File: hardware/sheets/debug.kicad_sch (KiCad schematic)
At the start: 0 parts

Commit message: hw: draw MCU module and debug sheets (#6)
* hw: draw MCU module and debug sheets

Draw the MDBT53-P1M with Raytac's normal-voltage DC/DC reference
circuit (Ver.E section 8.1.2): VDD and VDDH on 3V3 with 4.7 uF, a
10 uH inductor and 1 uF on each internal regulator output, and module
VBUS through 2.2 ohm with 4.7 uF. The 32.768 kHz crystal uses the
nRF5340's internal 9 pF load, with external load caps left unfitted.
USB D+/D- reach the module through 0 ohm links that can take the
27 ohm resistors shown in Raytac's figure.

The debug sheet has the ARM Cortex 10-pin SWD header and pads for
reset, SWD, UART, ground and six spare GPIO. The header connects to
the nRF5340 DK's debug out; pin 3 is grounded so the DK selects the
external target.

Labels whose other end belongs on a sheet not drawn yet are excluded
from ERC with a comment naming that sheet, to be removed as each
sheet is drawn.

* docs: describe the module supply and debug setup

Record the module's reference-circuit parts, the 0 ohm USB data links
and the SWD header in the hardware overview. State the DC/DC inductor
limits as TDK specifies them: 90 mA maximum for at most a 50%
inductance drop, with 250 mA only a typical temperature-rise
reference, against Nordic's reference BOM.

Debugging uses the nRF5340 DK's debug out. Nordic requires the target
voltage to match the DK, which runs at 3 V on USB alone, so bring-up
supplies the DK's nRF5340 with 3.3 V on its external input and checks
that the two voltages match before connecting. Bring-up also checks
the module's DC/DC regulators.

* ci: avoid SIGPIPE when printing host tool versions

Under pipefail, `--version | head -n 1` can fail the host-dependency
script when head exits before the tool finishes writing. Capture the
whole version output and print its first line instead.
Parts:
- added J501: SWD 2x5 1.27mm, Connector_PinHeader_1.27mm:PinHeader_2x05_P1.27mm_Vertical_SMD, symbol Connector:Conn_ARM_JTAG_SWD_10
- added TP501: nRESET, TestPoint:TestPoint_Pad_D1.0mm, symbol Connector:TestPoint
- added TP502: SWDIO, TestPoint:TestPoint_Pad_D1.0mm, symbol Connector:TestPoint
- added TP503: SWDCLK, TestPoint:TestPoint_Pad_D1.0mm, symbol Connector:TestPoint
- added TP504: UART_TX, TestPoint:TestPoint_Pad_D1.0mm, symbol Connector:TestPoint
- added TP505: UART_RX, TestPoint:TestPoint_Pad_D1.0mm, symbol Connector:TestPoint
- added TP506: GND, TestPoint:TestPoint_Pad_D1.0mm, symbol Connector:TestPoint
- added TP507: P0.02, TestPoint:TestPoint_Pad_D1.0mm, symbol Connector:TestPoint
- added TP508: P0.03, TestPoint:TestPoint_Pad_D1.0mm, symbol Connector:TestPoint
- added TP509: P0.13, TestPoint:TestPoint_Pad_D1.0mm, symbol Connector:TestPoint
- added TP510: P0.14, TestPoint:TestPoint_Pad_D1.0mm, symbol Connector:TestPoint
- added TP511: P0.26/AIN5, TestPoint:TestPoint_Pad_D1.0mm, symbol Connector:TestPoint
- added TP512: P0.27/AIN6, TestPoint:TestPoint_Pad_D1.0mm, symbol Connector:TestPoint
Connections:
- new net +3V3: J501.1 (VTref)
- new net GND: J501.3 (GND), J501.5 (GND), J501.9 (GNDDetect), TP506.1
- new net SPARE_P0_02: TP507.1
- new net SPARE_P0_03: TP508.1
- new net SPARE_P0_13: TP509.1
- new net SPARE_P0_14: TP510.1
- new net SPARE_P0_26: TP511.1
- new net SPARE_P0_27: TP512.1
- new net SWDCLK: J501.4 (SWCLK/TCK), TP503.1
- new net SWDIO: J501.2 (SWDIO/TMS), TP502.1
- new net UART_RX: TP505.1
- new net UART_TX: TP504.1
- new net nRESET: J501.10 (~{RESET}), TP501.1
- no-connect marks 0 -> 2
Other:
- note added: "Debug (Rev A) - design notes J501: ARM Cortex 10-pin SWD header (2 x 5, 1.27 mm) to the nRF5340 DK debug out (P19) by a 10-pin flat cable. Pin 3 = GND selects the external target. Voltages must match: run the DK at 3.3 V from P21 (SW10 VEXT->nRF ON, SW9 = VDD; DK on USB alone is 3.0 V). Keep DK SB47 open so P19 pin 1 does not drive the badge 3V3. VTref = 3V3; nRESET has the module's internal pull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"

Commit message: hw: apply layout footprint and test-point changes to the schematic
The matrix LEDs use the KENTO-pattern footprint, L1101 the PCB coil,
MK1001 the 0.6 mm hole footprint and J301 the project HRO copy.

Removes test points that duplicate others: TP303 and TP304, TP208 and
TP506, and TP501-TP503, whose signals are on the SWD header. Also
removes H1304, which the carrier does not use. Rail and GND test points
move to 0.8 mm pads.

nRESET now connects only the header's open-collector pin and the module
input. ERC reports that as not driven, so the error is excluded: the
nRF5340 has an internal pull-up on reset.
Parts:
- removed TP501: nRESET, TestPoint:TestPoint_Pad_D1.0mm, symbol Connector:TestPoint
- removed TP502: SWDIO, TestPoint:TestPoint_Pad_D1.0mm, symbol Connector:TestPoint
- removed TP503: SWDCLK, TestPoint:TestPoint_Pad_D1.0mm, symbol Connector:TestPoint
- removed TP506: GND, TestPoint:TestPoint_Pad_D1.0mm, symbol Connector:TestPoint

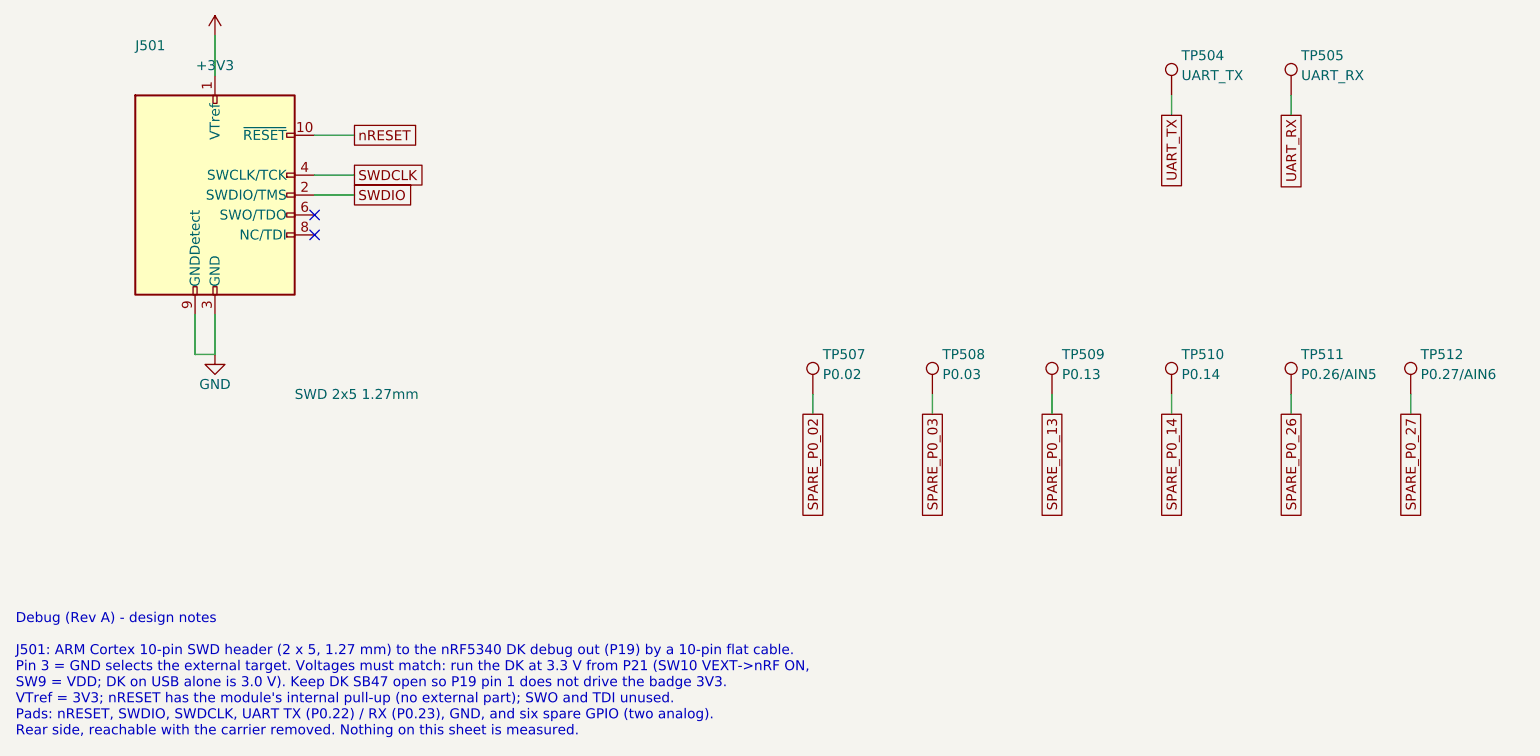
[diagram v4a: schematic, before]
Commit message: hw: switch U401 to the E73 nRF52840 module
The MDBT53-P1M cannot be sourced in time for the Rev A order, while
the E73-2G4M08S1C is stocked at JLCPCB (ADR 0015).

The E73 holds its DC/DC inductors and decoupling, so L401/L402 and
C403/C404 are removed. The nRF52840 has no internal 32.768 kHz load,
so C405/C406 are fitted with 12 pF; the value is calculated and still
needs checking against the Product Specification. All 29 module GPIO
are used: CHG_STAT is no longer read by the MCU, and the UART pads,
spare GPIO pads and IMU SPI-fallback links are removed. Pins Ebyte
marks as low-frequency carry only analog inputs or slow signals.
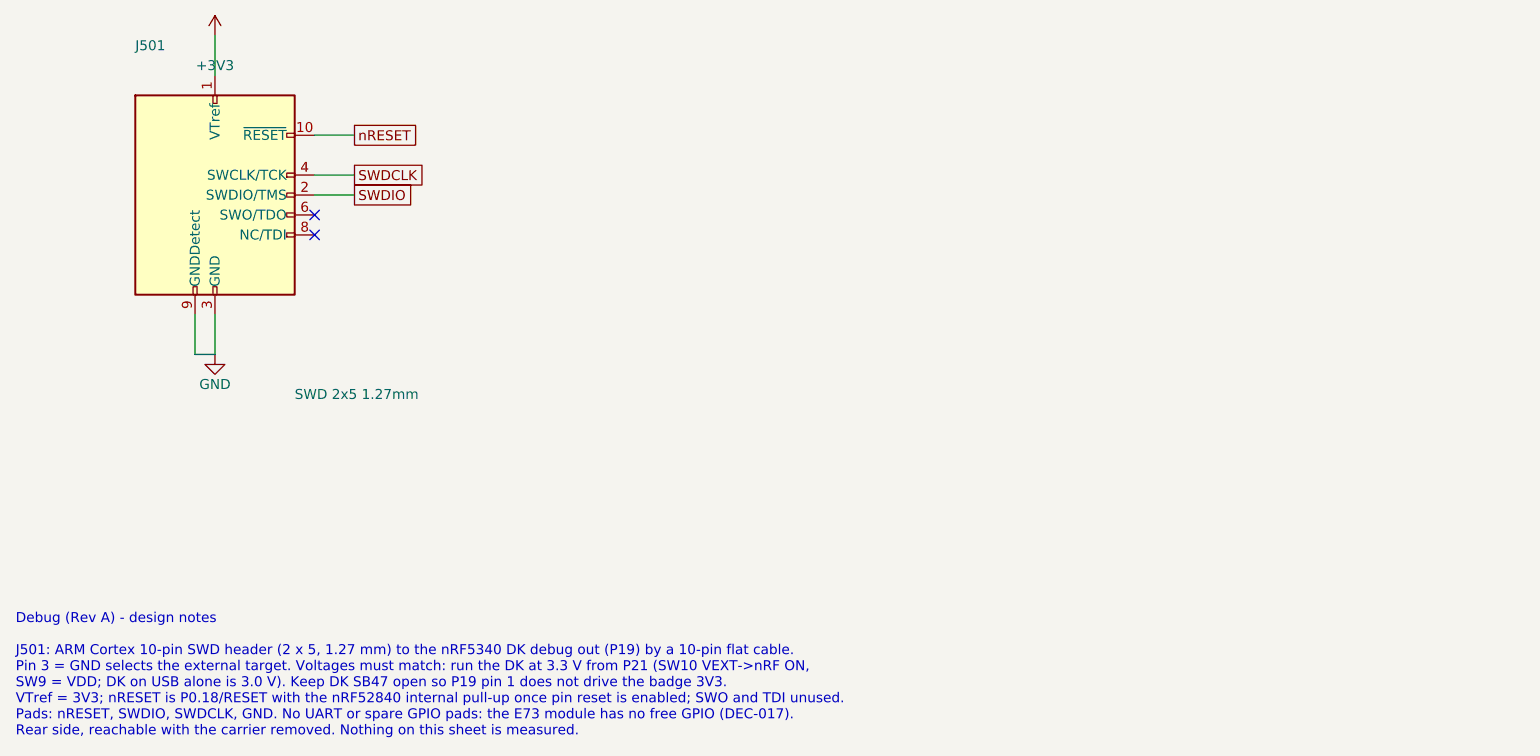
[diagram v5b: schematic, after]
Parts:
- removed TP504: UART_TX, TestPoint:TestPoint_Pad_D1.0mm, symbol Connector:TestPoint
- removed TP505: UART_RX, TestPoint:TestPoint_Pad_D1.0mm, symbol Connector:TestPoint
- removed TP507: P0.02, TestPoint:TestPoint_Pad_D1.0mm, symbol Connector:TestPoint
- removed TP508: P0.03, TestPoint:TestPoint_Pad_D1.0mm, symbol Connector:TestPoint
- removed TP509: P0.13, TestPoint:TestPoint_Pad_D1.0mm, symbol Connector:TestPoint
- removed TP510: P0.14, TestPoint:TestPoint_Pad_D1.0mm, symbol Connector:TestPoint
- removed TP511: P0.26/AIN5, TestPoint:TestPoint_Pad_D1.0mm, symbol Connector:TestPoint
- removed TP512: P0.27/AIN6, TestPoint:TestPoint_Pad_D1.0mm, symbol Connector:TestPoint
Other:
- note added: "Debug (Rev A) - design notes J501: ARM Cortex 10-pin SWD header (2 x 5, 1.27 mm) to the nRF5340 DK debug out (P19) by a 10-pin flat cable. Pin 3 = GND selects the external target. Voltages must match: run the DK at 3.3 V from P21 (SW10 VEXT->nRF ON, SW9 = VDD; DK on USB alone is 3.0 V). Keep DK SB47 open so P19 pin 1 does not drive the badge 3V3. VTref = 3V3; nRESET is P0.18/RESET with the nRF528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"
- note removed: "Debug (Rev A) - design notes J501: ARM Cortex 10-pin SWD header (2 x 5, 1.27 mm) to the nRF5340 DK debug out (P19) by a 10-pin flat cable. Pin 3 = GND selects the external target. Voltages must match: run the DK at 3.3 V from P21 (SW10 VEXT->nRF ON, SW9 = VDD; DK on USB alone is 3.0 V). Keep DK SB47 open so P19 pin 1 does not drive the badge 3V3. VTref = 3V3; nRESET has the module's internal pull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"
